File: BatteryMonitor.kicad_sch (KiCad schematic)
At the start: 17 parts, among them U3 MAX17205G+

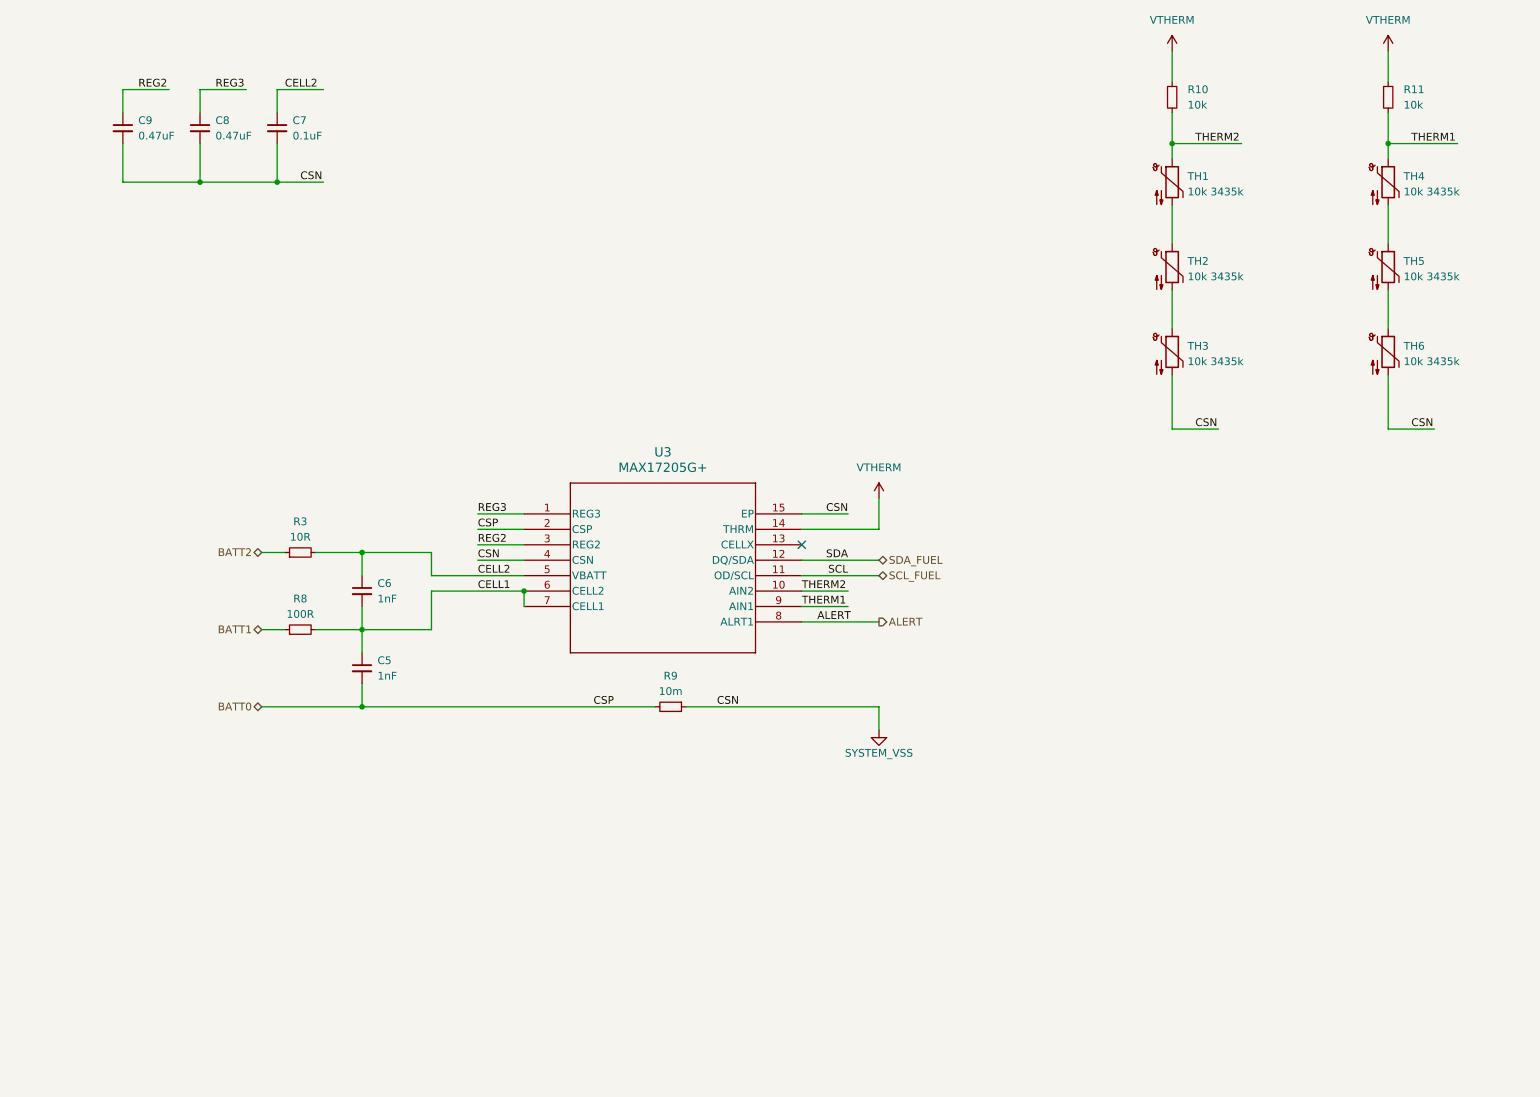
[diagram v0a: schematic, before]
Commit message: Refactored schematics and silkscreen
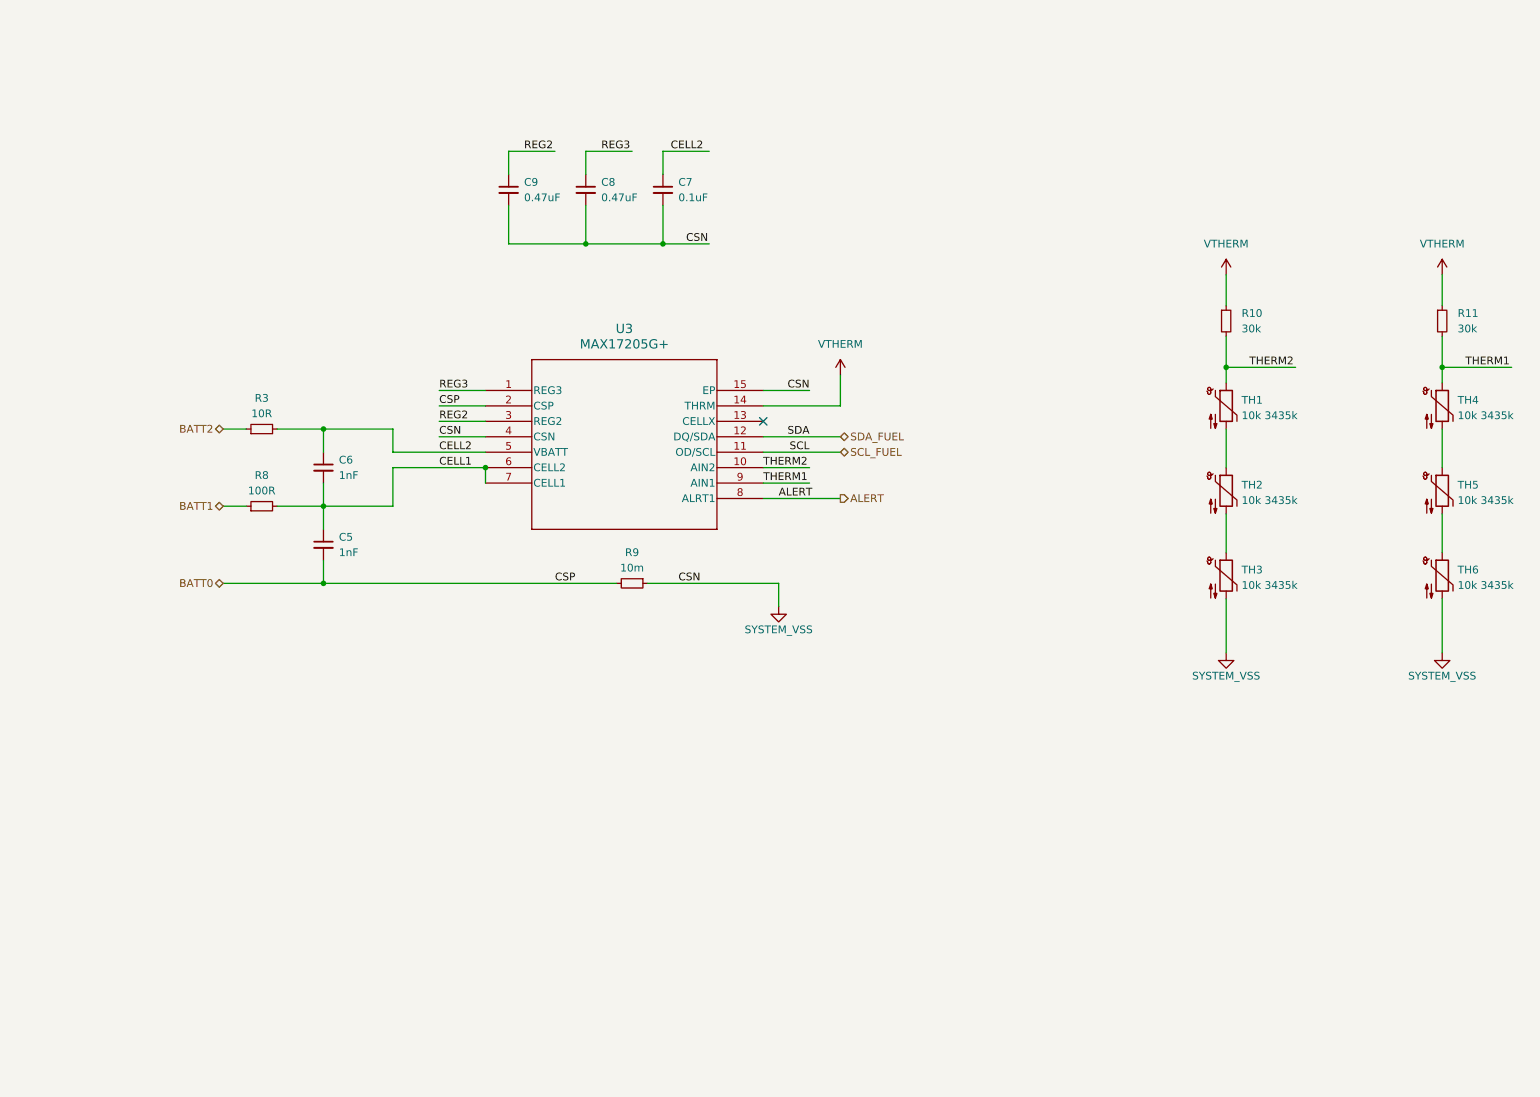
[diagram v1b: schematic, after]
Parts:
- C5, C6, C7, C8, C9, TH1, TH2, TH3, TH4, TH5, TH6: footprint (none) -> Capacitor_SMD:C_0603_1608Metric
- R10, R11: value 10k -> 30k; footprint (none) -> Resistor_SMD:R_0603_1608Metric
- R3, R8: footprint (none) -> Resistor_SMD:R_0603_1608Metric
- R9: footprint (none) -> Resistor_SMD:R_2512_6332Metric
- U3: footprint 21-0137_T1433+2C_MXM -> Battery-Board:21-0137_T1433&plus_2C_MXM
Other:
- moved on the sheet: C5, C6, C7, C8, C9, R10, R11, R3, R8, R9, TH1, TH2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

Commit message: Changes for lib refactor
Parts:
- U3: footprint Battery-Board:21-0137_T1433&plus_2C_MXM -> Argus-IC:21-0137_T1433&plus_2C_MXM; symbol Battery-Board:MAX17205G+ -> Argus-IC:MAX17205G+
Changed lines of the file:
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@@
 	)
 	(symbol
-		(lib_id "Battery-Board:MAX17205G+")
+		(lib_id "Argus-IC:MAX17205G+")
 		(at 92.71 85.09 0)
 		(unit 1)
@@
 			)
 		)
-		(property "Footprint" "Battery-Board:21-0137_T1433&plus_2C_MXM"
+		(property "Footprint" "Argus-IC:21-0137_T1433&plus_2C_MXM"
 			(at 92.71 85.09 0)
 			(effects

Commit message: v2.1 (v3?) Partial Updates
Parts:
- removed U3: MAX17205G+, Argus-IC:21-0137_T1433&plus_2C_MXM, symbol Argus-IC:MAX17205G+
- added J5: Fuel Gauge Programming Header, Connector_PinHeader_2.54mm:PinHeader_1x05_P2.54mm_Vertical_SMD_Pin1Left, symbol Connector_Generic:Conn_01x05
- added R51: 1k, Resistor_SMD:R_0603_1608Metric, symbol Device:R_Small
- added R54: 51.1k, Resistor_SMD:R_0603_1608Metric, symbol Device:R_Small
- added R55, R56, R57: 150R, Resistor_SMD:R_0603_1608Metric, symbol Device:R_Small
- added R58: 10k, Resistor_SMD:R_0603_1608Metric, symbol Device:R_Small
- added R59, R60: 0R, Resistor_SMD:R_0603_1608Metric, symbol Device:R_Small
- added U6: MAX17205, Package_DFN_QFN:TDFN-14-1EP_3x3mm_P0.4mm_EP1.78x2.35mm, symbol Argus-IC:MAX17205G
- renumbered C5 to C10, C7 to C11, C9 to C12, C8 to C13, C6 to C9, R3 to R48, R8 to R49, R9 to R50, R10 to R52, R11 to R53
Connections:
- net ALERT: now also R51.2, R54.1, R58.1
- net SYSTEM_VSS: now also J5.3 (Pin_3), U6.15 (GND), U6.4 (CSN)
- net BATT0 renamed BATT_N
- net BATT_N: now also U6.2 (CSP)
- net BATT1 renamed BATT_M
- net BATT2 renamed BATT_P
- net CELL1: no longer names the net of C10.1, C9.2, R49.2
- net CELL1: now also U6.6 (CELL2), U6.7 (CELL1)
- net CELL2: no longer names the net of C11.1, C9.1, R48.2
- net CELL2: now also U6.5 (VBATT)
- net REG2: no longer names the net of C12.1
- net REG2: now also U6.3 (REG2)
- net REG3: no longer names the net of C13.1
- net REG3: now also U6.1 (REG3)
- net THERM1: no longer names the net of R53.2, TH4.1
- net THERM1: now also U6.9 (AIN1)
- net THERM2: no longer names the net of R52.2, TH1.1
- net THERM2: now also U6.10 (AIN2)
- net VTHERM: no longer names the net of R52.1, R53.1
- net VTHERM: now also U6.14 (THRM)
- new net: R51.1, U6.8 (ALRT1)
- new net +3V3: R58.2
- new net A: J5.1 (Pin_1), R54.2
- new net C: J5.5 (Pin_5), R57.2
- new net D: J5.4 (Pin_4), R56.2
- new net DQ: J5.2 (Pin_2), R55.2
- new net I2C Protection/SCL_DEVICE: R59.2
- new net I2C Protection/SDA_DEVICE: R60.1
- new net SCL: R57.1, R59.1, U6.11 (SCL)
- new net SDA: R55.1, R56.1, R60.2, U6.12 (SDA)
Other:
- added sheet I2C Protection (I2CProtection.kicad_sch)
- note added: "Battery protection design derived from Portland State University's Open-Source OreSat project"
- note added: "Remove before programming"
- company: (none) -> Carnegie Mellon University
- title: (none) -> Argus Batteryboard
- moved on the sheet: C10, C11, C12, C13, C9, R48, R49, R50, R52, R53, TH1, TH2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

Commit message: Updated FPC connector
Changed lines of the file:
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@@
 (kicad_sch
-	(version 20231120)
+	(version 20250114)
 	(generator "eeschema")
-	(generator_version "8.0")
+	(generator_version "9.0")
 	(paper "USLetter")
 	(title_block
@@
 		(comment 3 "V. Rajesh")
 	)
+	(rectangle
+		(start 16.256 187.452)
+		(end 59.182 199.39)
+		(stroke
+			(width 0)
+			(type dash)
+		)
+		(fill
+			(type none)
+		)
+	)
+	(rectangle
+		(start 190.246 100.838)
+		(end 198.374 129.032)
+		(stroke
+			(width 0)
+			(type dash)
+		)
+		(fill
+			(type none)
+		)
+	)
+	(text "Remove before programming"
+		(exclude_from_sim no)
+		(at 195.072 131.064 0)
+		(effects
+			(font
+				(size 1.27 1.27)
+			)
+		)
+	)
+	(text "Battery protection design derived from \nPortland State University's \nOpen-Source OreSat project"
+		(exclude_from_sim no)
+		(at 37.846 193.548 0)
+		(effects
+			(font
+				(size 1.27 1.27)
+			)
+		)
+	)
 	(junction
 		(at 92.71 68.58)
@@
 		)
 	)
-	(rectangle
-		(start 16.256 187.452)
-		(end 59.182 199.39)
-		(stroke
-			(width 0)
-			(type dash)
-		)
-		(fill
-			(type none)
-		)
-	)
-	(rectangle
-		(start 190.246 100.838)
-		(end 198.374 129.032)
-		(stroke
-			(width 0)
-			(type dash)
-		)
-		(fill
-			(type none)
-		)
-	)
-	(text "Remove before programming"
-		(exclude_from_sim no)
-		(at 195.072 131.064 0)
-		(effects
-			(font
-				(size 1.27 1.27)
-			)
-		)
-	)
-	(text "Battery protection design derived from \nPortland State University's \nOpen-Source OreSat project"
-		(exclude_from_sim no)
-		(at 37.846 193.548 0)
-		(effects
-			(font
-				(size 1.27 1.27)
-			)
-		)
-	)
 	(label "C"
 		(at 215.9 82.55 180)
-		(fields_autoplaced yes)
 		(effects
 			(font
@@
 	(label "SCL"
 		(at 185.42 82.55 0)
-		(fields_autoplaced yes)
 		(effects
 			(font
@@
 	(label "SDA"
 		(at 185.42 121.92 0)
-		(fields_autoplaced yes)
 		(effects
 			(font
@@
 	(label "SDA"
 		(at 185.42 80.01 0)
-		(fields_autoplaced yes)
 		(effects
 			(font
@@
 	(label "SCL"
 		(at 132.08 81.28 180)
-		(fields_autoplaced yes)
 		(effects
 			(font
@@
 	(label "SDA"
 		(at 132.08 86.36 180)
-		(fields_autoplaced yes)
 		(effects
 			(font
@@
 	(label "SCL"
 		(at 185.42 116.84 0)
-		(fields_autoplaced yes)
 		(effects
 			(font
@@
 	(label "DQ"
 		(at 215.9 74.93 180)
-		(fields_autoplaced yes)
 		(effects
 			(font
@@
 	(label "D"
 		(at 215.9 80.01 180)
-		(fields_autoplaced yes)
 		(effects
 			(font
@@
 	(label "A"
 		(at 215.9 72.39 180)
-		(fields_autoplaced yes)
 		(effects
 			(font
@@
 	(label "SDA"
 		(at 185.42 74.93 0)
-		(fields_autoplaced yes)
 		(effects
 			(font
@@
 		(shape bidirectional)
 		(at 36.83 88.9 180)
-		(fields_autoplaced yes)
 		(effects
 			(font
@@
 		(shape bidirectional)
 		(at 36.83 109.22 180)
-		(fields_autoplaced yes)
 		(effects
 			(font
@@
 		(shape bidirectional)
 		(at 36.83 68.58 180)
-		(fields_autoplaced yes)
 		(effects
 			(font
@@
 		(shape output)
 		(at 185.42 106.68 180)
-		(fields_autoplaced yes)
 		(effects
 			(font
@@
 		(shape output)
 		(at 132.08 91.44 0)
-		(fields_autoplaced yes)
 		(effects
 			(font
@@
 		(shape bidirectional)
 		(at 36.83 99.06 180)
-		(fields_autoplaced yes)
 		(effects
 			(font
@@
 		(shape bidirectional)
 		(at 247.65 121.92 0)
-		(fields_autoplaced yes)
 		(effects
 			(font
@@
 		(shape output)
 		(at 185.42 72.39 180)
-		(fields_autoplaced yes)
 		(effects
 			(font
@@
 		(shape bidirectional)
 		(at 247.65 116.84 0)
-		(fields_autoplaced yes)
 		(effects
 			(font
@@
 		(at 203.2 114.3)
 		(size 38.1 10.16)
+		(exclude_from_sim no)
+		(in_bom yes)
+		(on_board yes)
+		(dnp no)
 		(fields_autoplaced yes)
 		(stroke
